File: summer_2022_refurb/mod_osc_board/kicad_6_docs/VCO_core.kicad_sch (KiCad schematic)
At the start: 37 parts, among them SW201 alpha_SR2612F-0112, U201 SSI2130, U202 TL072

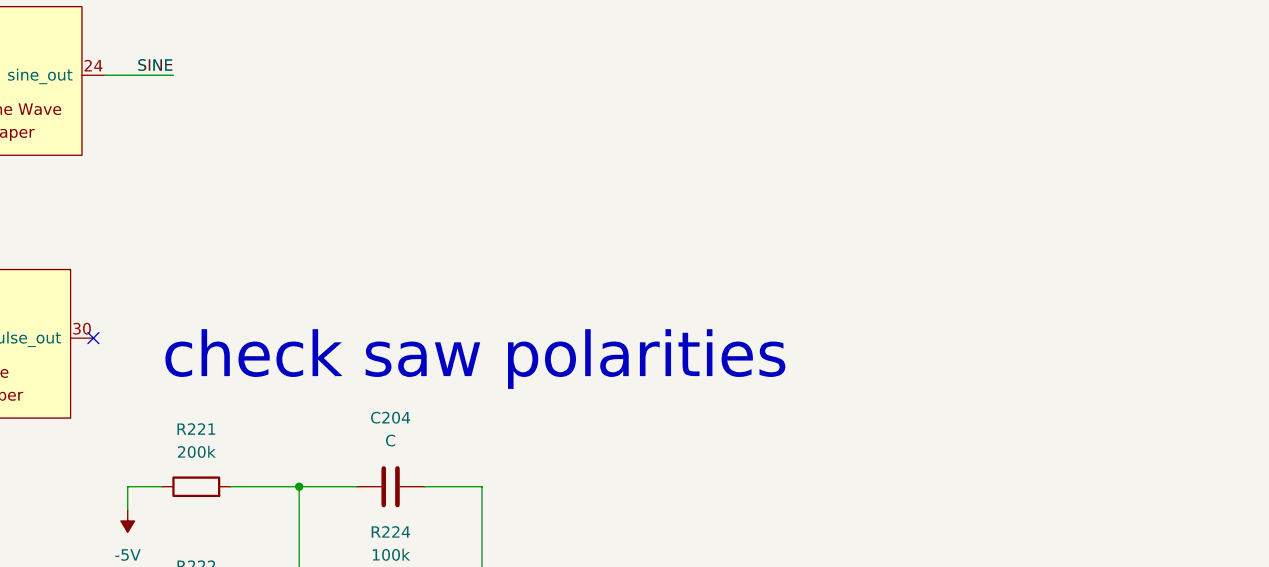
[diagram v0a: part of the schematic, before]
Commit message: Change directory structure, minor schem and pcb tweaks
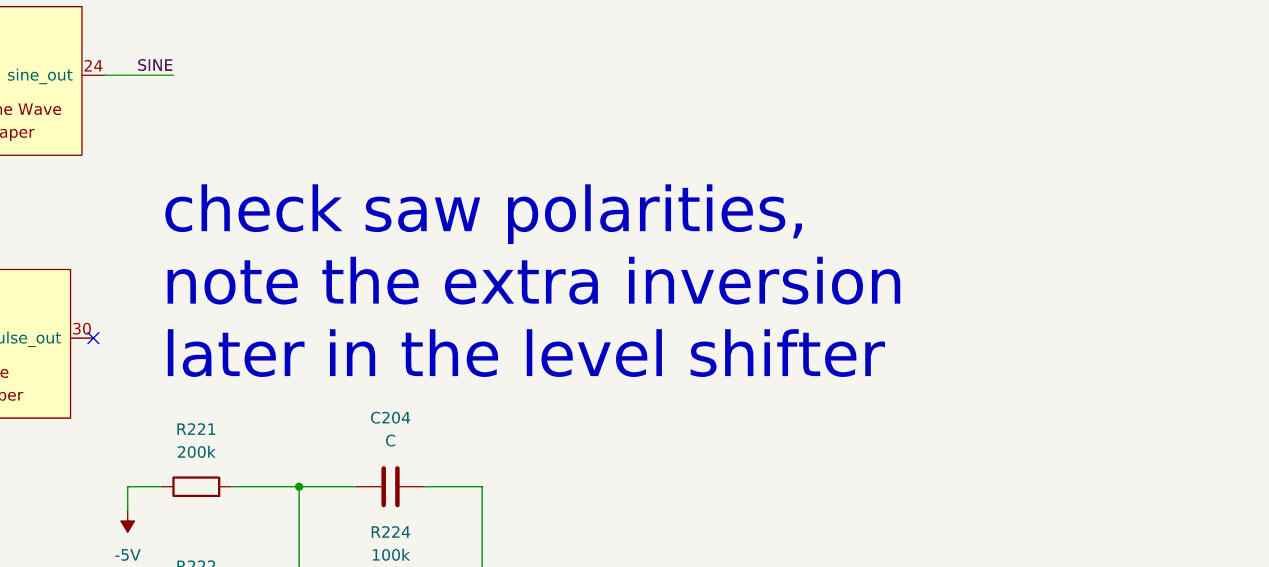
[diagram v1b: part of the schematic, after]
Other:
- note added: "check saw polarities, note the extra inversion later in the level shifter"
- note removed: "check saw polarities"
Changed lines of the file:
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@@
   (title_block
     (title "Josh Ox Ribbon Synth Mod Osc board")
-    (date "2022-06-12")
+    (date "2022-06-16")
     (rev "0")
     (comment 2 "creativecommons.org/licences/by/4.0")
@@
     (effects (font (size 1.27 1.27)) (justify left bottom))
   )
-  (text "check saw polarities" (at 219.71 72.39 0)
+  (text "check saw polarities,\nnote the extra inversion\nlater in the level shifter"
+    (at 219.71 72.39 0)
     (effects (font (size 5 5)) (justify left bottom))
   )

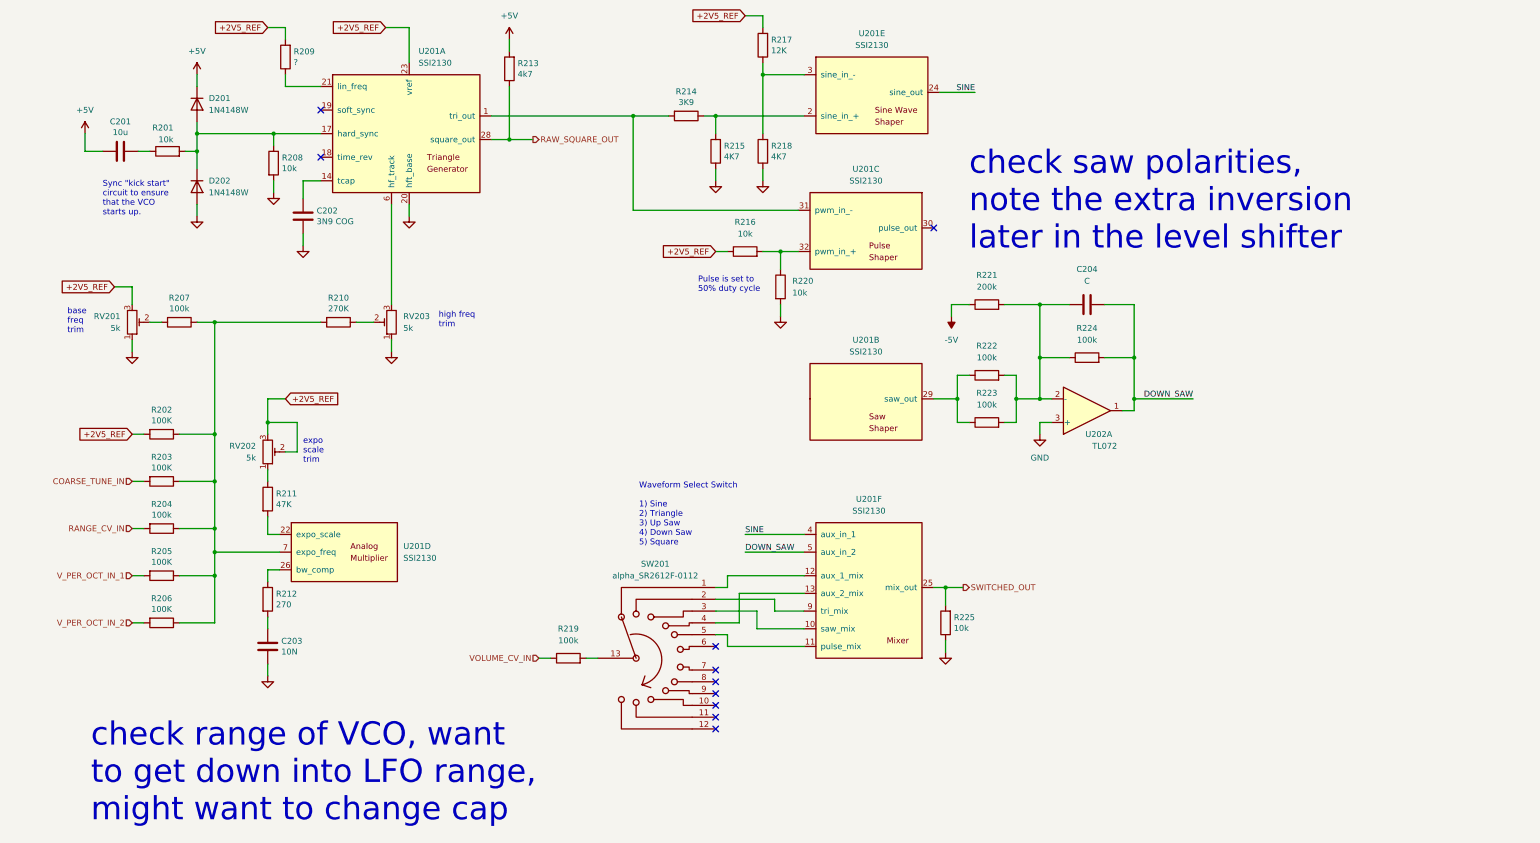
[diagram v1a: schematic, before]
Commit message: Buffer square, add saw polarity jumper
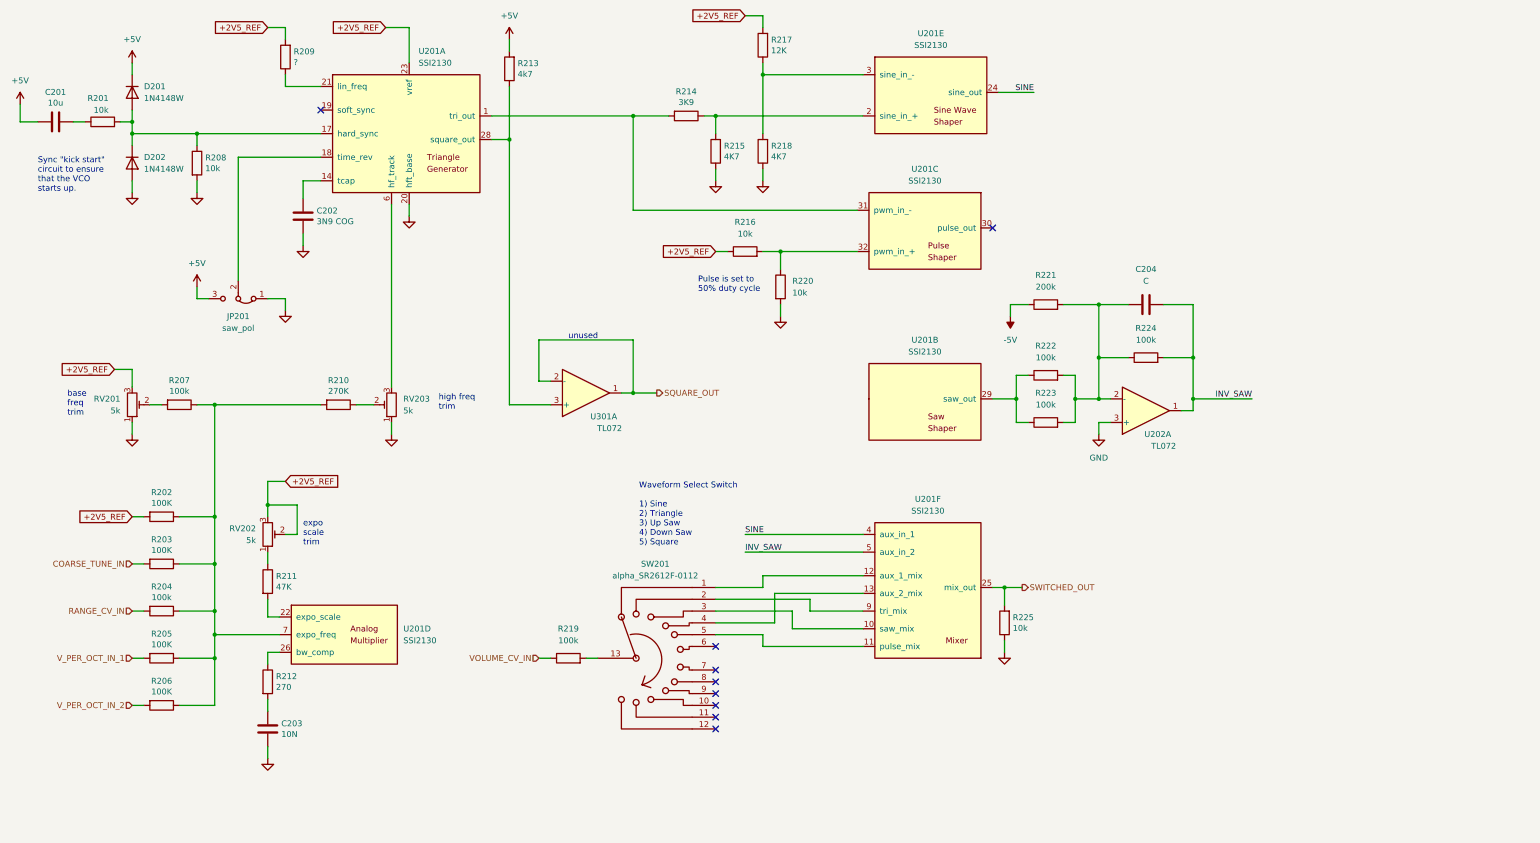
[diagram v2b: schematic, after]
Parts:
- added JP201: saw_pol, Jumper:SolderJumper-3_P1.3mm_Bridged12_RoundedPad1.0x1.5mm, symbol Jumper:Jumper_3_Bridged12
- added U301: TL072, Package_SO:SO-8_5.3x6.2mm_P1.27mm, symbol Amplifier_Operational:TL072
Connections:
- net +5V: now also JP201.3 (B)
- net GND: now also JP201.1 (A)
- net at U201.18 (time_rev): now also JP201.2 (C)
- net DOWN_SAW renamed INV_SAW
- net RAW_SQUARE_OUT: no longer names the net of R213.1, U201.28 (square_out)
- net RAW_SQUARE_OUT: now also U301.3 (+)
- new net SQUARE_OUT: U301.1, U301.2 (-)
- no-connect marks 10 -> 9
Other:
- note added: "unused"
- note removed: "check range of VCO, want to get down into LFO range, might want to change cap"
- note removed: "check saw polarities, note the extra inversion later in the level shifter"
- moved on the sheet: C201, C203, C204, D201, D202, R201, R202, R203, R204, R205, R206, R207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
